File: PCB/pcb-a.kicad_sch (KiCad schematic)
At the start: 23 parts, among them Q1 BC337, Q2 BC337, Q3 BC337, Q4 BC337, SW1 SW_DIP_x02, U1 MCP23008-xP, U4 ATmega16L-8P

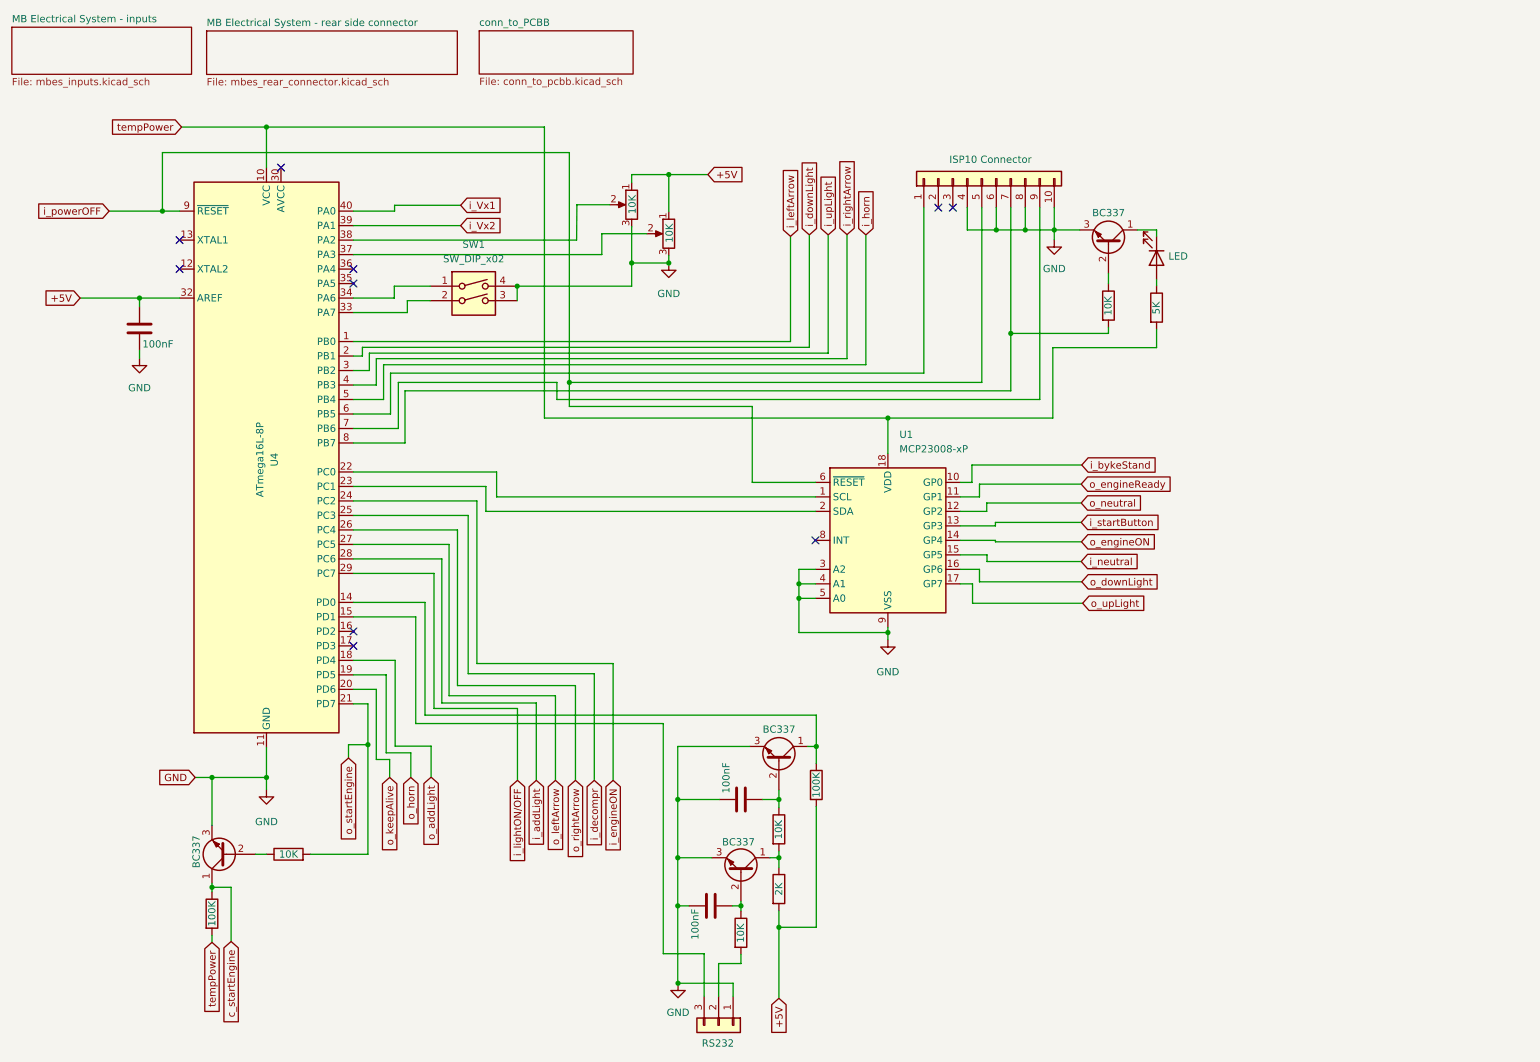
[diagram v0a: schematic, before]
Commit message: Refactoring: only not critical I/O on MCP23008XP
I know also MCP23008XP is under military standards, but I want my motorbike still be usable after the MCP23008XP is broken
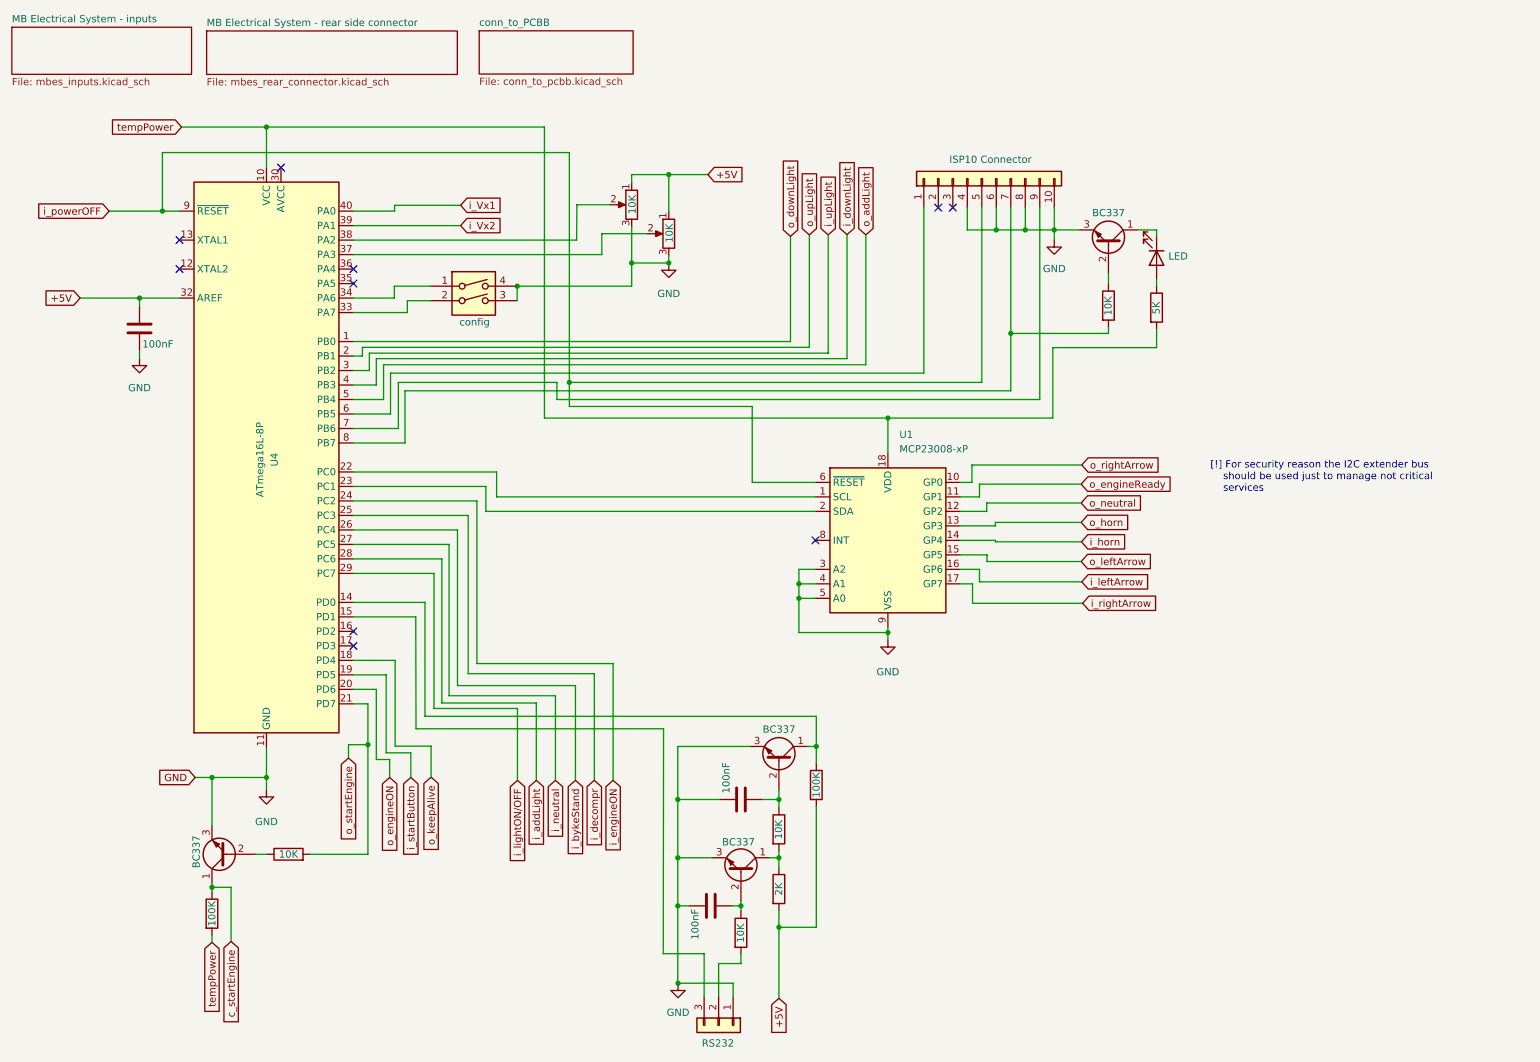
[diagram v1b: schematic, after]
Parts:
- SW1: value SW_DIP_x02 -> config
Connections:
- net i_bykeStand: now also U4.26 (PC4); no longer U1.10 (GP0)
- net i_downLight: now also U4.4 (PB3); no longer U4.2 (PB1)
- net i_horn: now also U1.14 (GP4); no longer U4.5 (PB4)
- net i_leftArrow: now also U1.16 (GP6); no longer U4.1 (PB0)
- net i_neutral: now also U4.27 (PC5); no longer U1.15 (GP5)
- net i_rightArrow: now also U1.17 (GP7); no longer U4.4 (PB3)
- net i_startButton: now also U4.19 (PD5); no longer U1.13 (GP3)
- net o_addLight: now also U4.5 (PB4); no longer U4.18 (PD4)
- net o_downLight: now also U4.1 (PB0); no longer U1.16 (GP6)
- net o_engineON: now also U4.20 (PD6); no longer U1.14 (GP4)
- net o_horn: now also U1.13 (GP3); no longer U4.19 (PD5)
- net o_keepAlive: now also U4.18 (PD4); no longer U4.20 (PD6)
- net o_leftArrow: now also U1.15 (GP5); no longer U4.27 (PC5)
- net o_rightArrow: now also U1.10 (GP0); no longer U4.26 (PC4)
- net o_upLight: now also U4.2 (PB1); no longer U1.17 (GP7)
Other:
- note added: "[!] For security reason the I2C extender bus should be used just to manage not critical services"

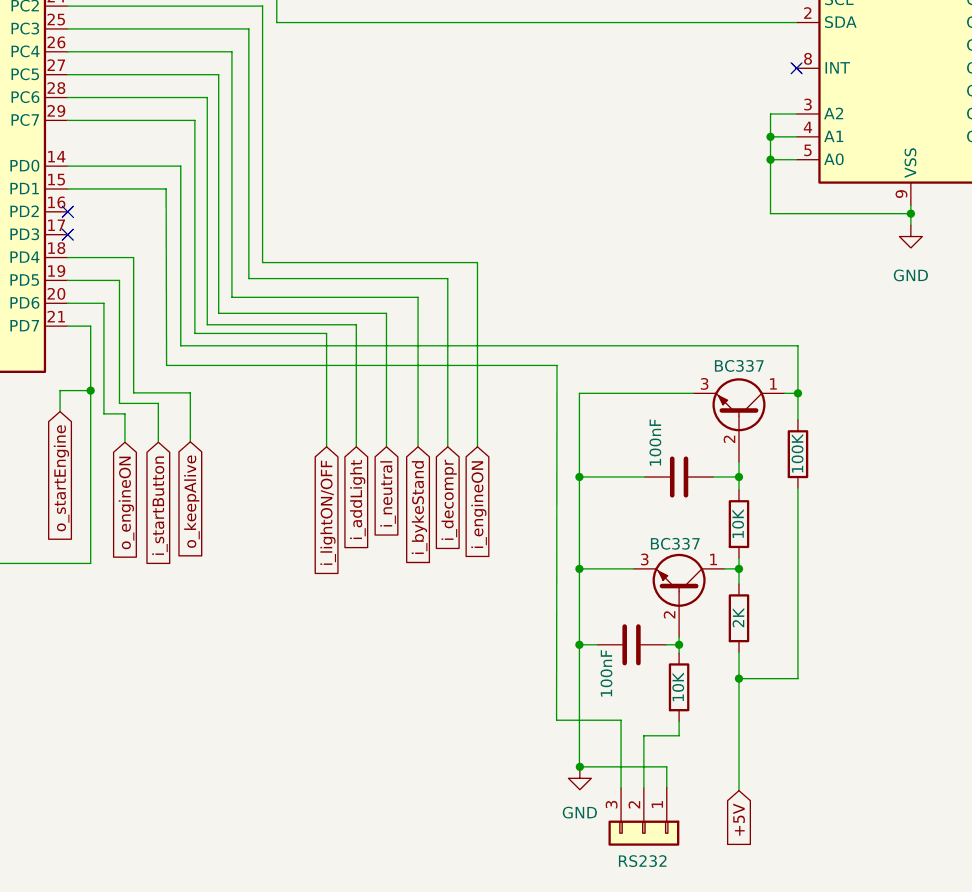
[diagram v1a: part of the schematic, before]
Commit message: Unusefull components removing and RS232 connected also to PCB-b
- The low-pass filter on RS232 RXD has been removed because external serial cable idea has been dropped
- The RS232 lines are been connected also to the PCB-b for future (CH5 module) Bluetooth implementation
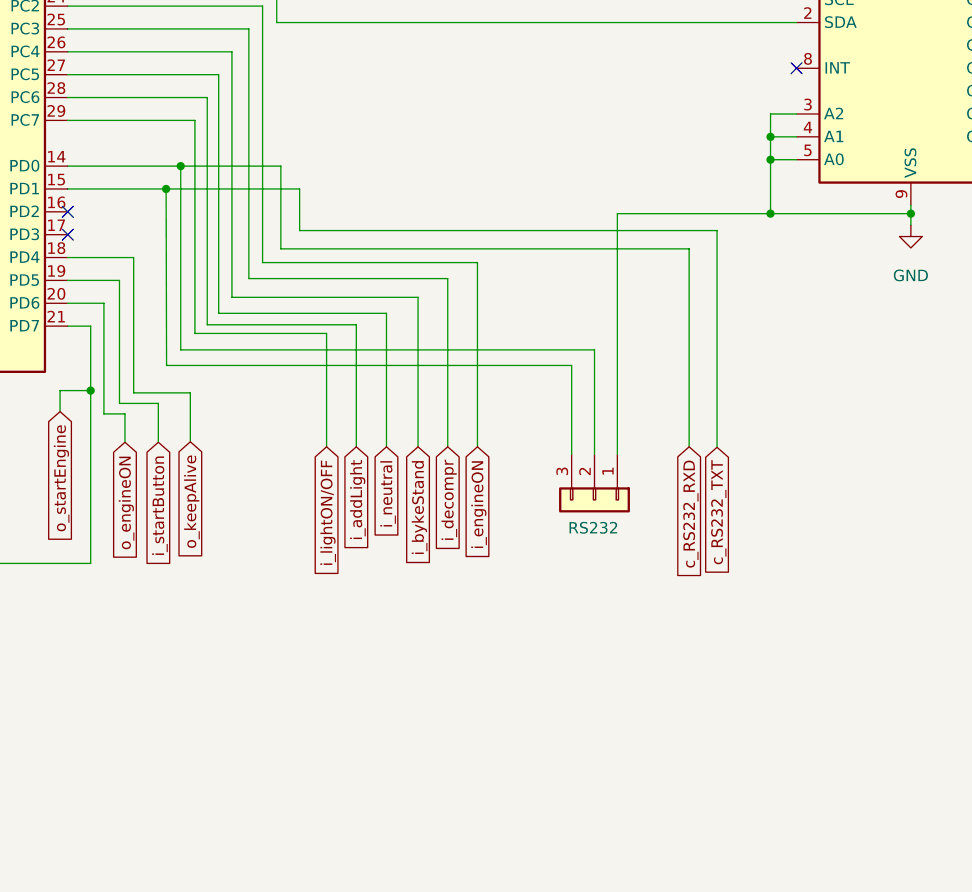
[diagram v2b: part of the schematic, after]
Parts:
- removed C1, C3: 100nF, Capacitor_THT:C_Disc_D6.0mm_W2.5mm_P5.00mm, symbol Device:C
- removed Q1, Q2: BC337, Package_TO_SOT_THT:TO-92_Inline_Wide, symbol Transistor_BJT:BC337
- removed R2, R3: 10K, Resistor_THT:R_Axial_DIN0207_L6.3mm_D2.5mm_P7.62mm_Horizontal, symbol Device:R
- removed R4: 2K, Resistor_THT:R_Axial_DIN0207_L6.3mm_D2.5mm_P7.62mm_Horizontal, symbol Device:R
- removed R5: 100K, Resistor_THT:R_Axial_DIN0207_L6.3mm_D2.5mm_P7.62mm_Horizontal, symbol Device:R
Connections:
- net c_RS232_RXD: now reaches U4.14 (PD0)
- net c_RS232_RXD: now also RS232-1.2 (Pin_2)
- net c_RS232_TXT: now reaches RS232-1.3 (Pin_3), U4.15 (PD1)

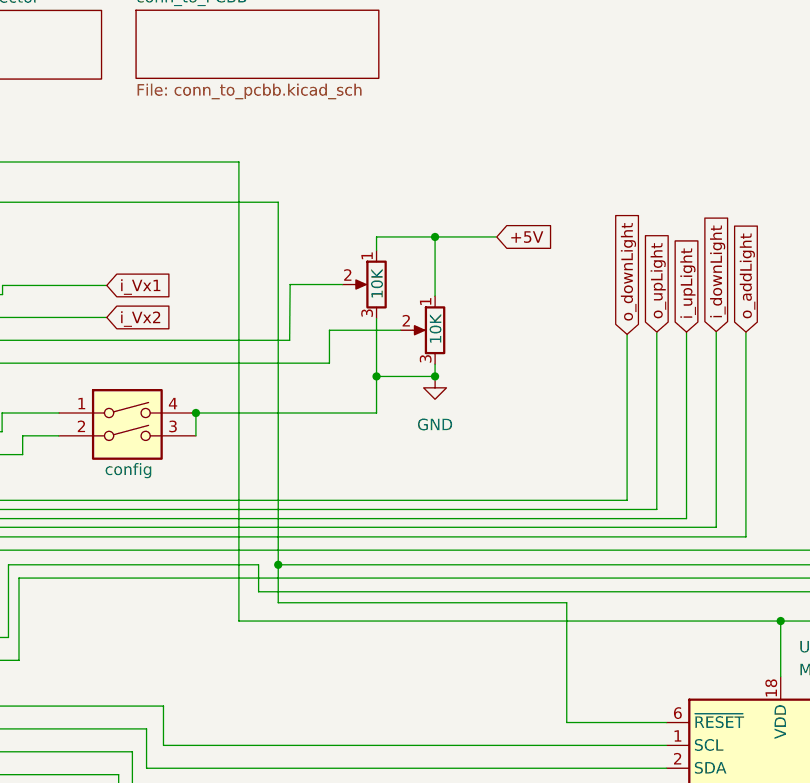
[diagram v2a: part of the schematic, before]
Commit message: Less wasted electric power when mb is turned off
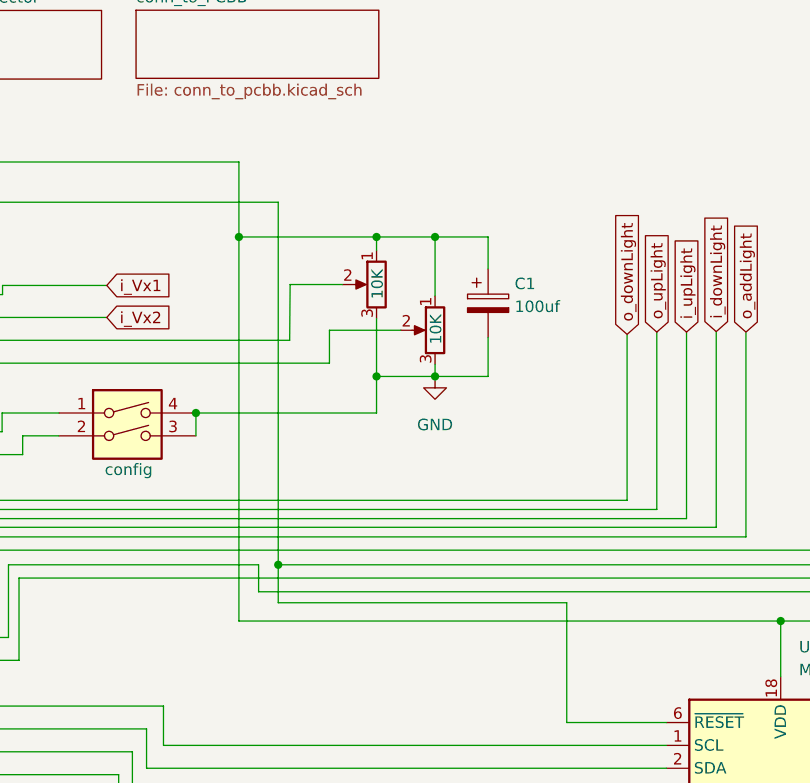
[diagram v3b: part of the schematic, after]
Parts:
- added C1: 100uf, Capacitor_THT:CP_Radial_D8.0mm_P2.50mm, symbol Device:C_Polarized
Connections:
- net +5V: no longer RV1.1, RV2.1
- net GND: now also C1.2
- net tempPower: now also RV1.1, RV2.1, C1.1
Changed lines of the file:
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@@
   (junction (at 36.83 65.278) (diameter 0) (color 0 0 0 0)
+  )
+  (junction (at 123.0884 43.6372) (diameter 0) (color 0 0 0 0)
+  )
+  (junction (at 107.7976 43.6372) (diameter 0) (color 0 0 0 0)
   )
   (junction (at 86.868 118.618) (diameter 0) (color 0 0 0 0)
@@
     (stroke (width 0) (type default) (color 0 0 0 0))
   )
+  (wire (pts (xy 107.7976 43.6372) (xy 123.0884 43.6372))
+    (stroke (width 0) (type default) (color 0 0 0 0))
+  )
   (wire (pts (xy 57.15 162.7632) (xy 59.1312 162.7632))
     (stroke (width 0) (type default) (color 0 0 0 0))
@@
     (stroke (width 0) (type default) (color 0 0 0 0))
   )
+  (wire (pts (xy 107.7976 43.6372) (xy 107.7976 35.306))
+    (stroke (width 0) (type default) (color 0 0 0 0))
+  )
   (wire (pts (xy 192.0748 53.34) (xy 186.9948 53.34))
     (stroke (width 0) (type default) (color 0 0 0 0))
@@
     (stroke (width 0) (type default) (color 0 0 0 0))
   )
+  (wire (pts (xy 135.4836 59.1312) (xy 129.5908 59.1312))
+    (stroke (width 0) (type default) (color 0 0 0 0))
+  )
   (wire (pts (xy 132.842 139.0396) (xy 132.842 150.622))
     (stroke (width 0) (type default) (color 0 0 0 0))
@@
     (stroke (width 0) (type default) (color 0 0 0 0))
   )
+  (wire (pts (xy 135.4836 43.6372) (xy 129.5908 43.6372))
+    (stroke (width 0) (type default) (color 0 0 0 0))
+  )
   (wire (pts (xy 167.9956 122.9868) (xy 167.9956 123.9012))
     (stroke (width 0) (type default) (color 0 0 0 0))
@@
     (stroke (width 0) (type default) (color 0 0 0 0))
   )
-  (wire (pts (xy 107.7976 86.3092) (xy 107.7976 35.306))
+  (wire (pts (xy 107.7976 86.3092) (xy 107.7976 43.6372))
     (stroke (width 0) (type default) (color 0 0 0 0))
   )
@@
     (stroke (width 0) (type default) (color 0 0 0 0))
   )
-  (wire (pts (xy 129.5908 43.6372) (xy 136.4488 43.6372))
-    (stroke (width 0) (type default) (color 0 0 0 0))
-  )
   (wire (pts (xy 73.4568 143.5608) (xy 76.8604 143.5608))
     (stroke (width 0) (type default) (color 0 0 0 0))
@@
     (stroke (width 0) (type default) (color 0 0 0 0))
   )
+  (wire (pts (xy 135.4836 47.1932) (xy 135.4836 43.6372))
+    (stroke (width 0) (type default) (color 0 0 0 0))
+  )
   (wire (pts (xy 182.8292 118.7704) (xy 202.1332 118.7704))
     (stroke (width 0) (type default) (color 0 0 0 0))
@@
   )
   (wire (pts (xy 112.1664 80.0608) (xy 184.4548 80.0608))
+    (stroke (width 0) (type default) (color 0 0 0 0))
+  )
+  (wire (pts (xy 135.4836 54.8132) (xy 135.4836 59.1312))
     (stroke (width 0) (type default) (color 0 0 0 0))
   )
@@
     (property "Riferimenti inter-foglio" "${INTERSHEET_REFS}" (id 0) (at 116.6146 161.8985 90)
       (effects (font (size 1.27 1.27)) (justify right) hide)
-    )
-  )
-  (global_label "+5V" (shape input) (at 136.4488 43.6372 0) (fields_autoplaced)
-    (effects (font (size 1.27 1.27)) (justify left))
-    (property "Riferimenti inter-foglio" "${INTERSHEET_REFS}" (id 0) (at 142.7324 43.5578 0)
-      (effects (font (size 1.27 1.27)) (justify left) hide)
     )
   )
@@
     (pin "2")
   )
+  (symbol (lib_id "Device:C_Polarized") (at 135.4836 51.0032 0) (unit 1)
+    (in_bom yes) (on_board yes) (fields_autoplaced)
+    (property "Reference" "C1" (id 0) (at 138.43 48.8441 0)
+      (effects (font (size 1.27 1.27)) (justify left))
+    )
+    (property "Value" "100uf" (id 1) (at 138.43 51.3841 0)
+      (effects (font (size 1.27 1.27)) (justify left))
+    )
+    (property "Footprint" "Capacitor_THT:CP_Radial_D8.0mm_P2.50mm" (id 2) (at 136.4488 54.8132 0)
+      (effects (font (size 1.27 1.27)) hide)
+    )
+    (property "Datasheet" "~" (id 3) (at 135.4836 51.0032 0)
+      (effects (font (size 1.27 1.27)) hide)
+    )
+    (pin "1")
+    (pin "2")
+  )
   (symbol (lib_id "Device:R_Potentiometer") (at 129.5908 54.0004 0) (mirror y) (unit 1)
     (in_bom yes) (on_board yes)
@@
       (reference "Bike_stand1") (unit 1) (value "Conn_01x02") (footprint "Connector_Wire:SolderWire-0.5sqmm_1x02_P4.6mm_D0.9mm_OD2.1mm")
     )
+    (path "/a3838906-f80d-4767-97ae-ce6a718330cb"
+      (reference "C1") (unit 1) (value "100uf") (footprint "Capacitor_THT:CP_Radial_D8.0mm_P2.50mm")
+    )
     (path "/30686728-a02e-4504-8ee7-08ed90242c91"
